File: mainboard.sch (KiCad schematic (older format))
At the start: 13 parts

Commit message: Added notes/toDo file, swapped xMEGA for a model from kicad standard library
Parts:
- removed IC?: XMEGA_A3B, atmel-TQFP44, symbol XMEGA_A3B
- added IC?: ATXMEGA256A3U-A, TQFP64, symbol ATXMEGA256A3U-A
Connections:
- net labels added: E2_DIR, E2_EN, E2_STEP, X_DIR, X_EN, X_STEP, Y_DIR, Y_EN, Y_STEP, Z_DIR, Z_EN, Z_STEP
- wire segments 45 -> 58
- no-connect marks 2 -> 0
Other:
- note added: "END STOPS"
- note added: "USB"
- note removed: "ENDSTOPS"
- note removed: "Extruder Control"
- note removed: "PORT B: ADCB"
- note removed: "Port A: ADCA"
- moved on the sheet: K?, P?, R?

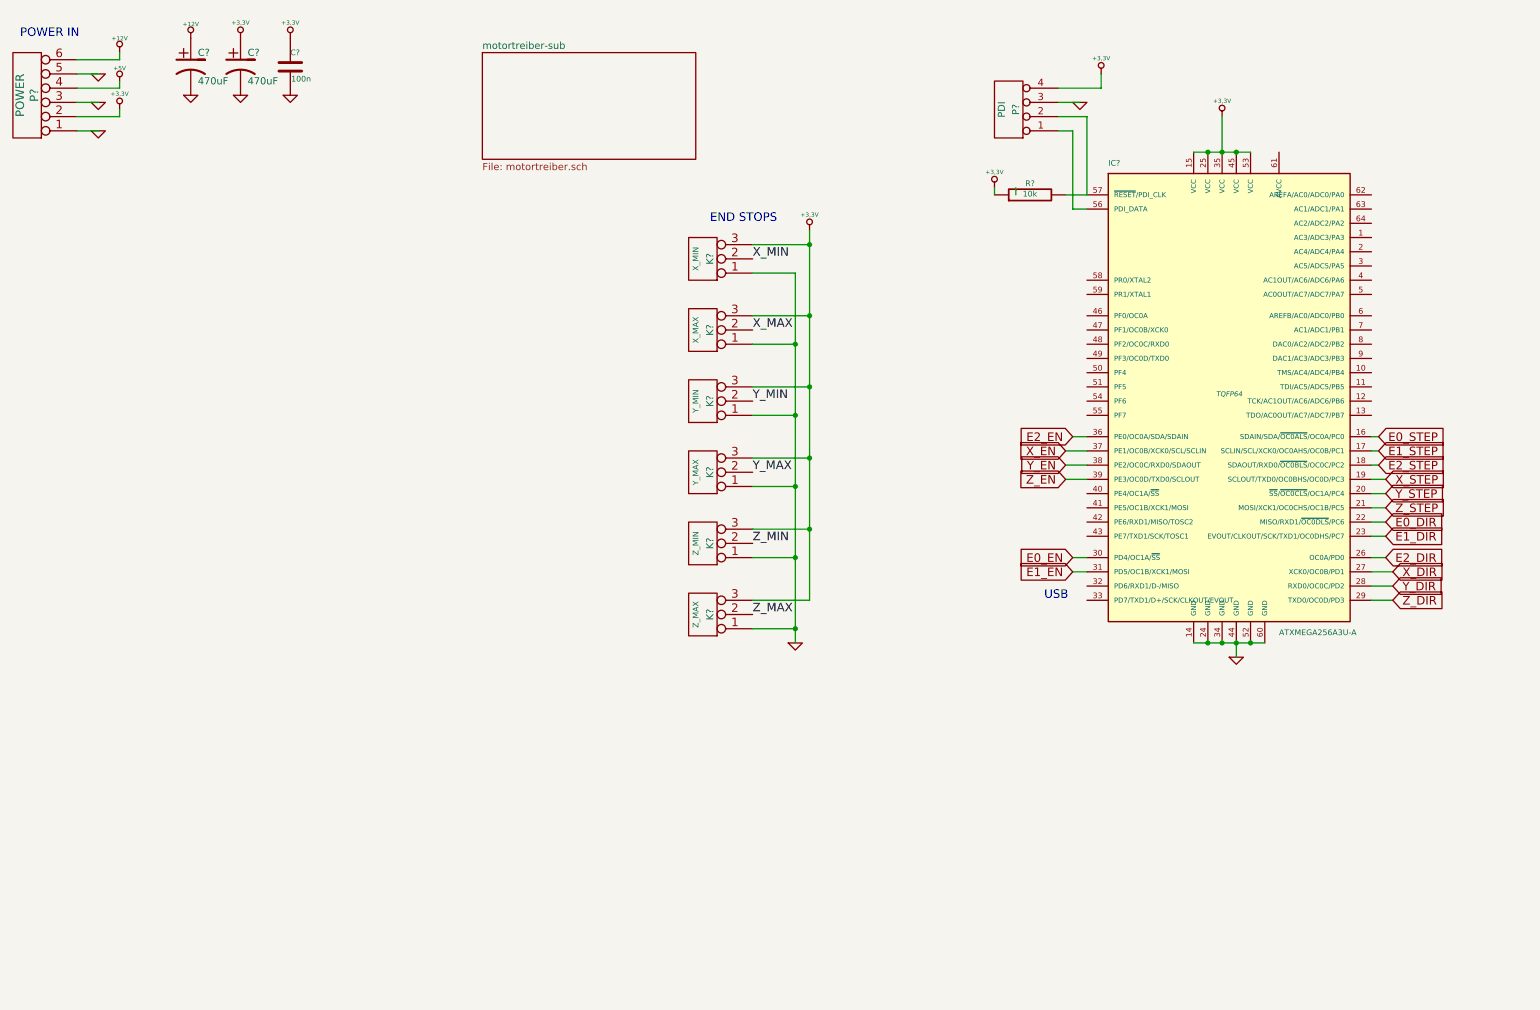
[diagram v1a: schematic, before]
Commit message: Added a bunch of new labels to the microcontroller
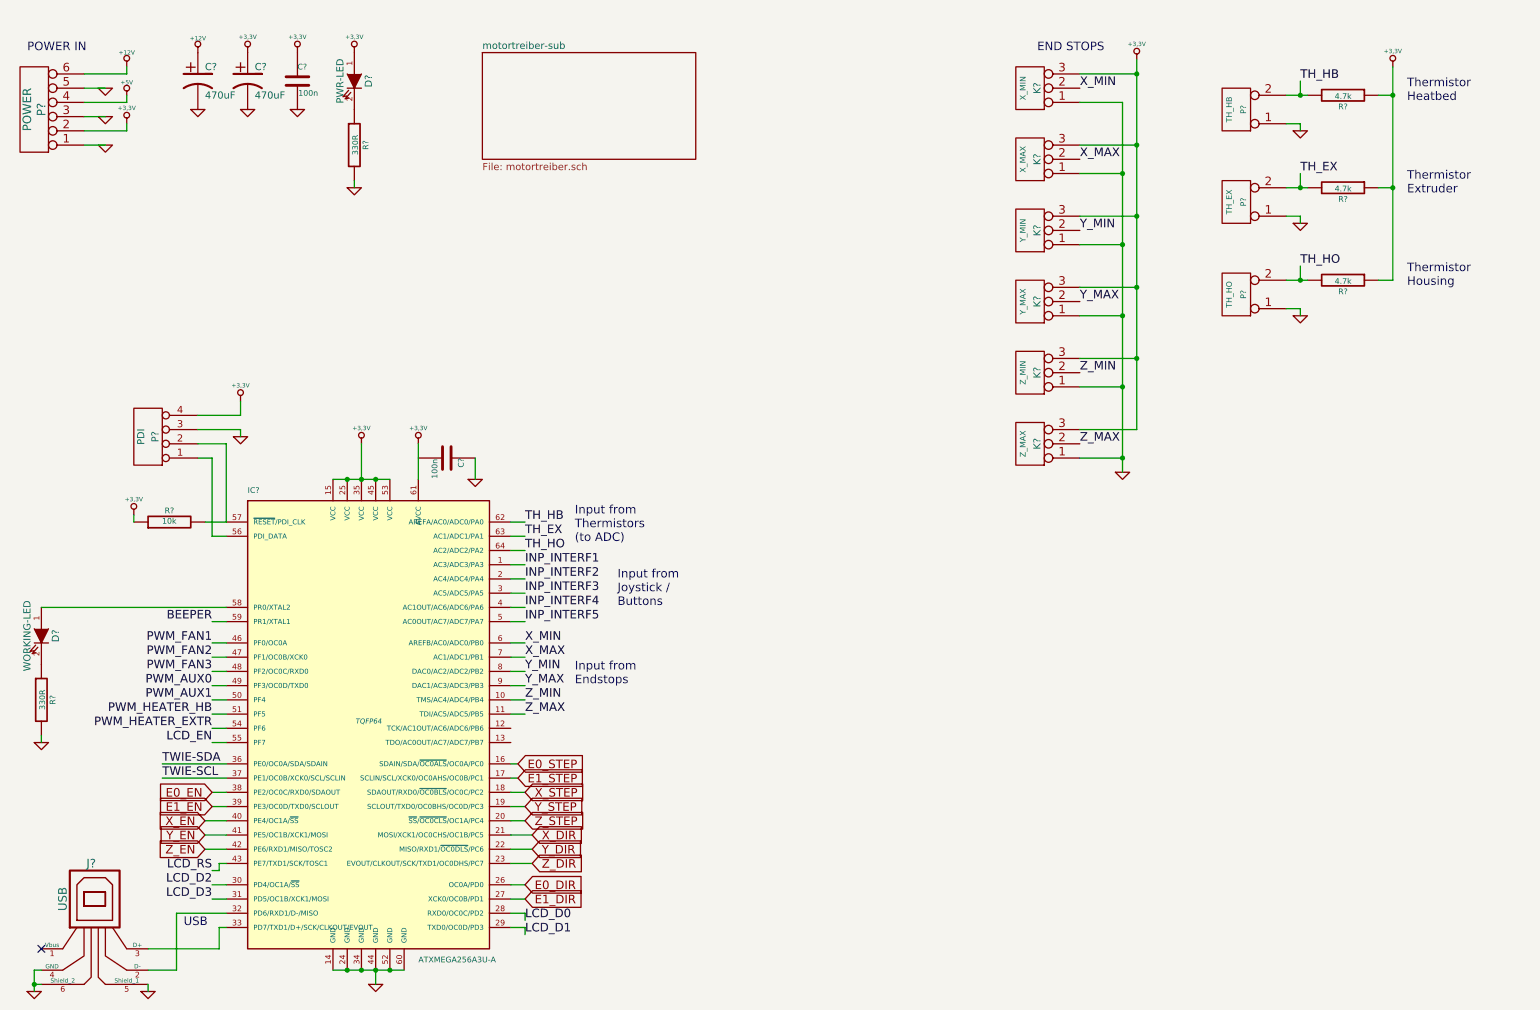
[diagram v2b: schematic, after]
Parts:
- added C?: 100n, ~, symbol C
- added D?: PWR-LED, symbol LED
- added D?: WORKING-LED, symbol LED
- added J?: USB, symbol USB
- added P?: TH_HB, symbol CONN_2
- added P?: TH_EX, symbol CONN_2
- added P?: TH_HO, symbol CONN_2
- added R? (x3): 4.7k, symbol R
- added R? (x2): 330R, symbol R
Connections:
- net E2_DIR is gone; now on net E0_DIR: IC?.26 (OC0A/PD0)
- net E2_STEP is gone; now on net X_STEP: IC?.18 (SDAOUT/RXD0/~OC0BLS~/OC0C/PC2)
- net +3.3V: now also IC?.61 (AVCC), D?.1 (A), R?.1, R?.1, R?.1
- net E0_DIR: no longer IC?.22 (MISO/RXD1/~OC0DLS~/PC6)
- net E0_EN: now also IC?.38 (PE2/OC0C/RXD0/SDAOUT); no longer IC?.30 (PD4/OC1A/~SS~)
- net E1_DIR: now also IC?.27 (XCK0/OC0B/PD1); no longer IC?.23 (EVOUT/CLKOUT/SCK/TXD1/OC0DHS/PC7)
- net E1_EN: now also IC?.39 (PE3/OC0D/TXD0/SCLOUT); no longer IC?.31 (PD5/OC1B/XCK1/MOSI)
- net GND: now also C?.1, J?.4 (GND), J?.5 (Shield_1), J?.6 (Shield_2), P?.1 (P1), P?.1 (P1), P?.1 (P1), R?.2, R?.2
- net X_DIR: now also IC?.21 (MOSI/XCK1/OC0CHS/OC1B/PC5); no longer IC?.27 (XCK0/OC0B/PD1)
- net X_EN: now also IC?.40 (PE4/OC1A/~SS~); no longer IC?.37 (PE1/OC0B/XCK0/SCL/SCLIN)
- net X_MAX: now also IC?.7 (AC1/ADC1/PB1)
- net X_MIN: now also IC?.6 (AREFB/AC0/ADC0/PB0)
- net X_STEP: no longer IC?.19 (SCLOUT/TXD0/OC0BHS/OC0D/PC3)
- net Y_DIR: now also IC?.22 (MISO/RXD1/~OC0DLS~/PC6); no longer IC?.28 (RXD0/OC0C/PD2)
- net Y_EN: now also IC?.41 (PE5/OC1B/XCK1/MOSI); no longer IC?.38 (PE2/OC0C/RXD0/SDAOUT)
- net Y_MAX: now also IC?.9 (DAC1/AC3/ADC3/PB3)
- net Y_MIN: now also IC?.8 (DAC0/AC2/ADC2/PB2)
- net Y_STEP: now also IC?.19 (SCLOUT/TXD0/OC0BHS/OC0D/PC3); no longer IC?.20 (~SS~/~OC0CLS~/OC1A/PC4)
- net Z_DIR: now also IC?.23 (EVOUT/CLKOUT/SCK/TXD1/OC0DHS/PC7); no longer IC?.29 (TXD0/OC0D/PD3)
- net Z_EN: now also IC?.42 (PE6/RXD1/MISO/TOSC2); no longer IC?.39 (PE3/OC0D/TXD0/SCLOUT)
- net Z_MAX: now also IC?.11 (TDI/AC5/ADC5/PB5)
- net Z_MIN: now also IC?.10 (TMS/AC4/ADC4/PB4)
- net Z_STEP: now also IC?.20 (~SS~/~OC0CLS~/OC1A/PC4); no longer IC?.21 (MOSI/XCK1/OC0CHS/OC1B/PC5)
- net INP_INTERF1: now reaches IC?.1 (AC3/ADC3/PA3)
- net INP_INTERF2: now reaches IC?.2 (AC4/ADC4/PA4)
- net INP_INTERF3: now reaches IC?.3 (AC5/ADC5/PA5)
- net at IC?.32 (PD6/RXD1/D-/MISO): now also J?.2 (D-)
- net at IC?.33 (PD7/TXD1/D+/SCK/CLKOUT/EVOUT): now also J?.3 (D+)
- net INP_INTERF4: now reaches IC?.4 (AC1OUT/AC6/ADC6/PA6)
- net LCD_RS: now reaches IC?.43 (PE7/TXD1/SCK/TOSC1)
- net PWM_FAN1: now reaches IC?.46 (PF0/OC0A)
- net PWM_FAN2: now reaches IC?.47 (PF1/OC0B/XCK0)
- net PWM_FAN3: now reaches IC?.48 (PF2/OC0C/RXD0)
- net PWM_AUX0: now reaches IC?.49 (PF3/OC0D/TXD0)
- net INP_INTERF5: now reaches IC?.5 (AC0OUT/AC7/ADC7/PA7)
- net PWM_AUX1: now reaches IC?.50 (PF4)
- net PWM_HEATER_HB: now reaches IC?.51 (PF5)
- net PWM_HEATER_EXTR: now reaches IC?.54 (PF6)
- net LCD_EN: now reaches IC?.55 (PF7)
- net at IC?.58 (PR0/XTAL2): now also D?.1 (A)
- net BEEPER: now reaches IC?.59 (PR1/XTAL1)
- net TH_HB: now reaches IC?.62 (AREFA/AC0/ADC0/PA0)
- net TH_HB: now also P?.2 (PM), R?.2
- net TH_EX: now reaches IC?.63 (AC1/ADC1/PA1)
- net TH_EX: now also P?.2 (PM), R?.2
- net TH_HO: now reaches IC?.64 (AC2/ADC2/PA2)
- net TH_HO: now also P?.2 (PM), R?.2
- net E2_EN renamed TWIE-SDA
- new net: D?.2 (K), R?.1 (x2)
- new net LCD_D0: IC?.28 (RXD0/OC0C/PD2)
- new net LCD_D1: IC?.29 (TXD0/OC0D/PD3)
- new net LCD_D2: IC?.30 (PD4/OC1A/~SS~)
- new net LCD_D3: IC?.31 (PD5/OC1B/XCK1/MOSI)
- new net TWIE-SCL: IC?.37 (PE1/OC0B/XCK0/SCL/SCLIN)
- no-connect marks 0 -> 1
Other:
- note added: "Input from\nEndstops"
- note added: "Input from\nJoystick / \nButtons"
- note added: "Input from\nThermistors \n(to ADC)"
- note added: "Thermistor\nExtruder"
- note added: "Thermistor\nHeatbed"
- note added: "Thermistor\nHousing"
- moved on the sheet: C?, IC?, K?, P?, R?

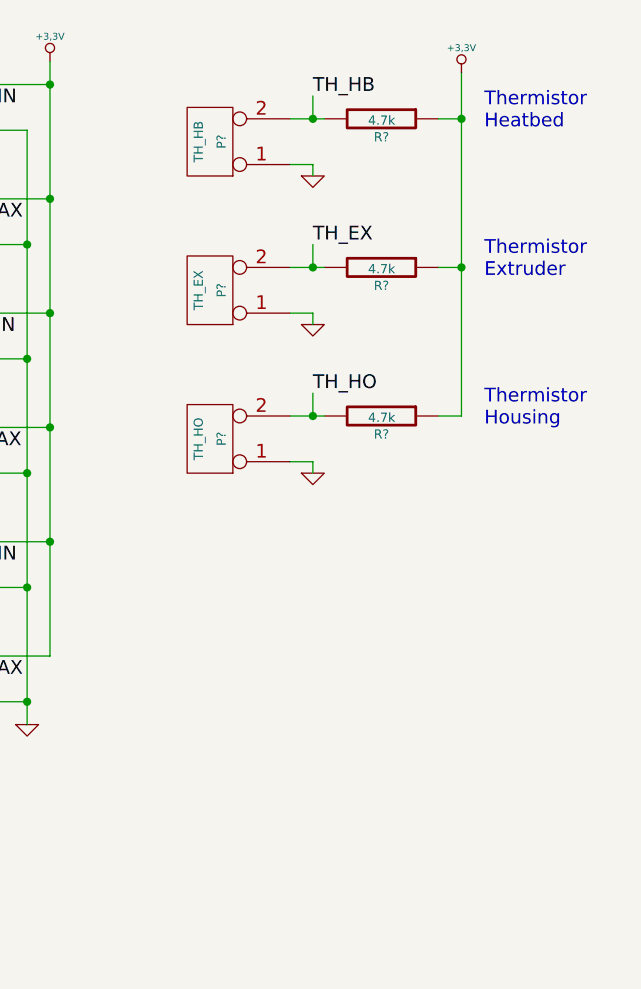
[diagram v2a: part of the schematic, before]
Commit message: removed 1 stepper motor driver (-> to have enough ports left for the LCD), added low pass filters to thermistor inputs
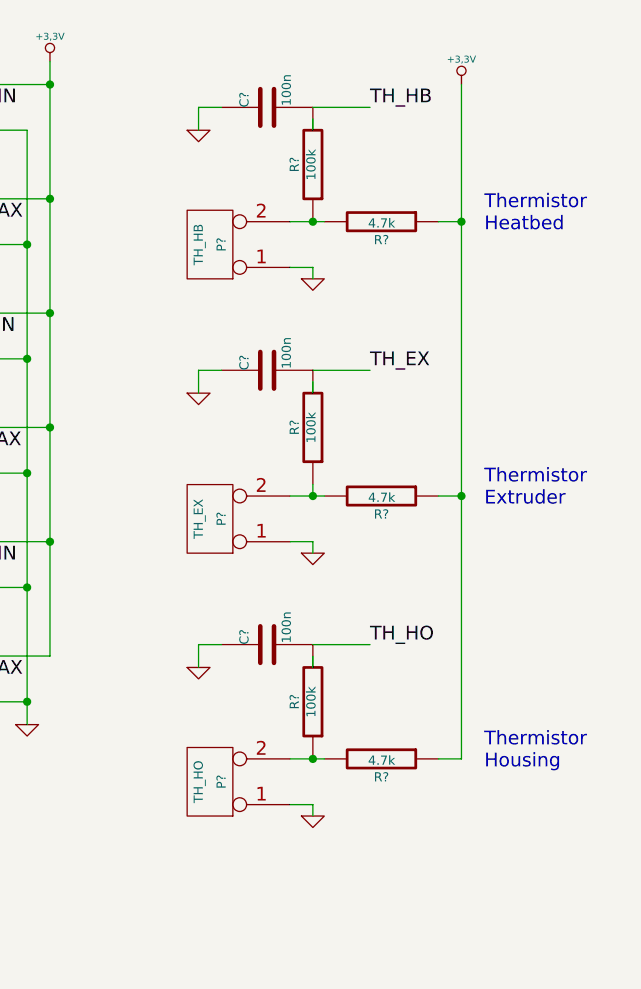
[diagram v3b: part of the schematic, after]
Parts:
- added C? (x3): 100n, symbol C
- added R? (x3): 100k, symbol R
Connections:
- wire segments 120 -> 130
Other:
- moved on the sheet: P?, R?

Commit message: Added LCD connector (pin assignment for connector tbd). Added 555 timer circuit for beeper (400Hz)
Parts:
- added C?: 1uF, ~, symbol CP1
- added C?: 100n, ~, symbol C
- added C?: 10n, ~, symbol C
- added P?: DISPLAY, symbol CONN_10
- added P?: BEEPER, symbol CONN_2
- added Q?: BCV 27 SMD, symbol NPN
- added R?: 330, symbol R
- added R?: 18k, symbol R
- added R?: 2.2k, symbol R
- added RV?: POT, symbol POT
- added U?: LM555N, symbol LM555N
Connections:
- net labels added: GND_555, LCD_CONTR, LCD_D4, LCD_D5, LCD_D6, LCD_D7, LCD_RW
- net labels removed: LCD_D0, LCD_D1, LCD_D2, LCD_D3
- wire segments 130 -> 170
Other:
- note added: "Circuit creates apprx. 400Hz beep"
- note added: "Low-pass:\nfC=480Hz"
- moved on the sheet: C?, D?, K?, P?, R?
